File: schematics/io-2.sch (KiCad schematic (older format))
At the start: 9 parts, among them J13 FDC Connector, J9 IDE Connector, U11 WD1772

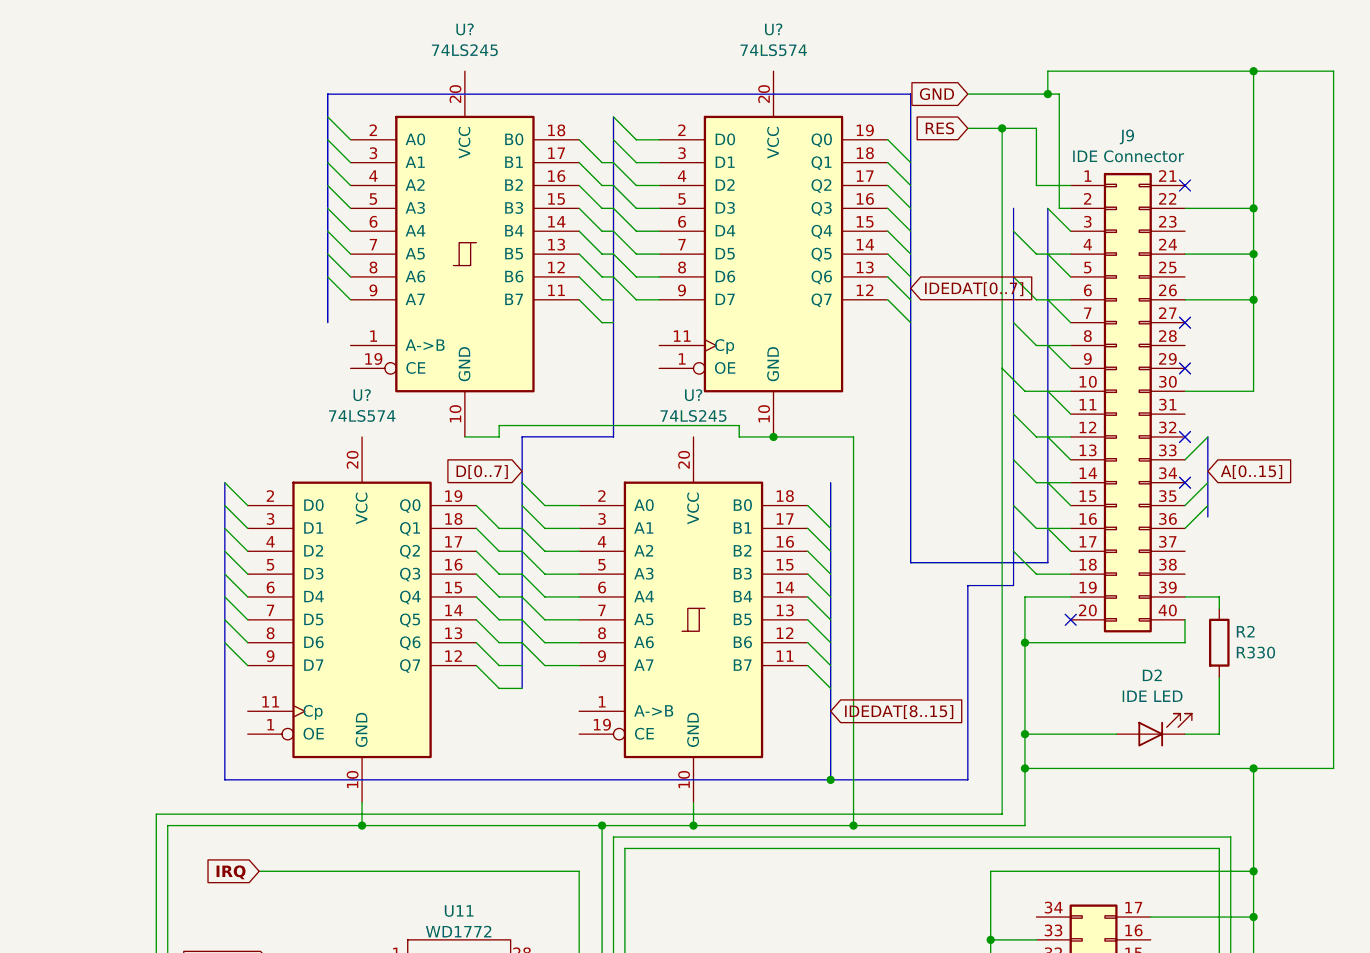
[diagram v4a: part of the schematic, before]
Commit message: Added missing IDE control signals for the latches, bus drivers, reads/writes and chip selects.
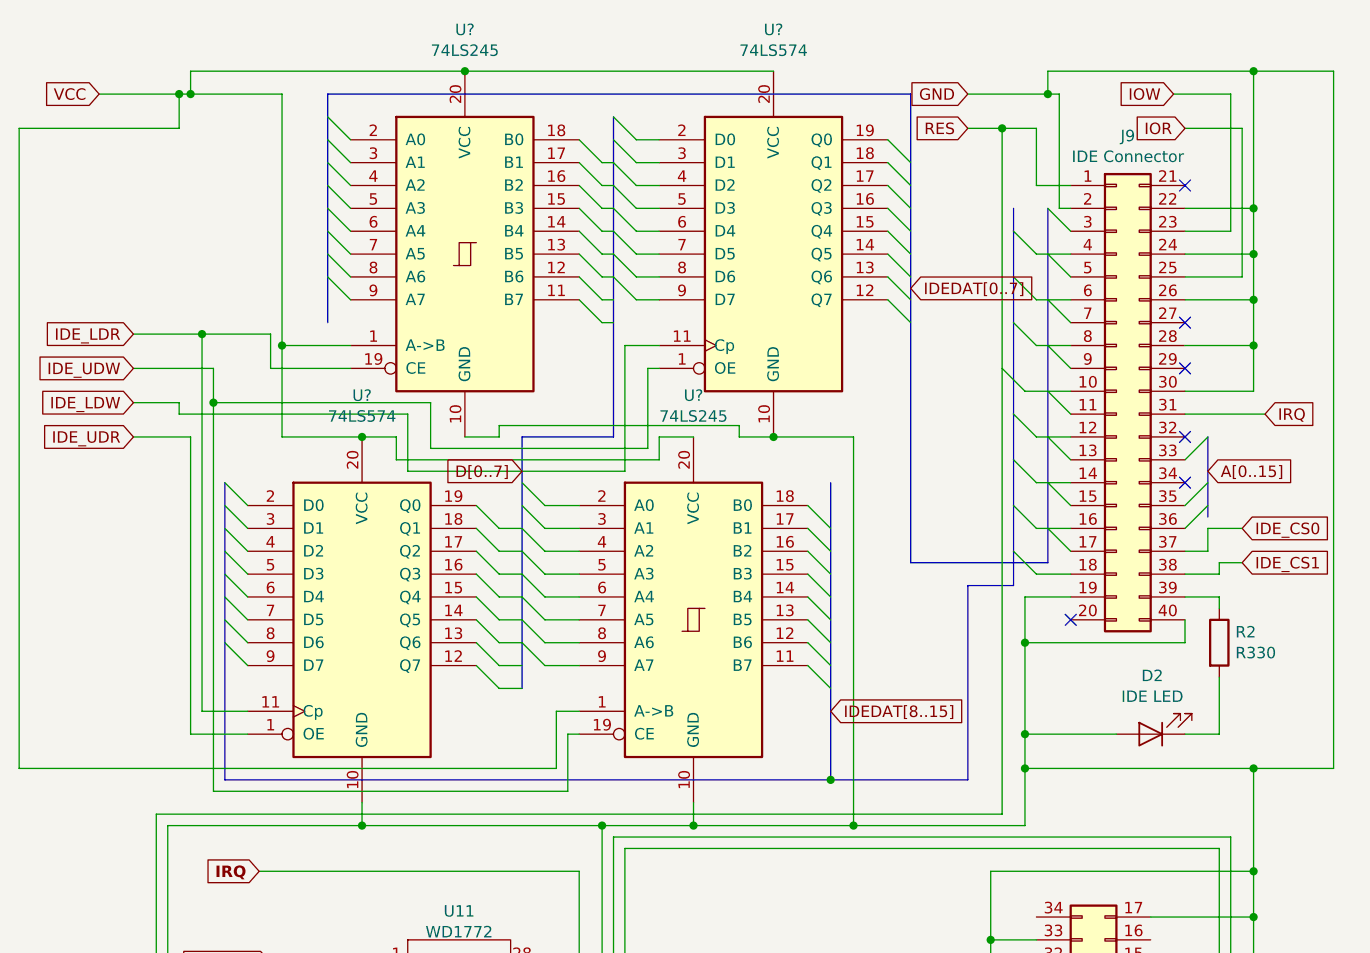
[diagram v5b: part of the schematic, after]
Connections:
- net D[0..7]: now also U?.11 (Cp)
- net GND: now also J9.28 (Pin_28)
- net IRQ: now also J9.31 (Pin_31)
- net VCC: now also U?.1 (A->B), U?.1 (A->B), U?.20 (VCC), U?.20 (VCC), U?.20 (VCC), U?.20 (VCC)
- net IOW: now reaches J9.23 (Pin_23)
- net IOR: now reaches J9.25 (Pin_25)
- net IDE_CS0: now reaches J9.37 (Pin_37)
- net IDE_CS1: now reaches J9.38 (Pin_38)
- net IDE_UDW: now reaches U?.1 (OE)
- net IDE_UDW: now also U?.19 (CE)
- net IDE_UDR: now reaches U?.1 (OE)
- net IDE_LDR: now reaches U?.11 (Cp)
- net IDE_LDR: now also U?.19 (CE)
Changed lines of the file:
@@
 	10500 1950 10800 1950
 Wire Wire Line
-	10800 1950 10800 1550
+	10800 1950 10800 1750
 Connection ~ 10800 1550
 Wire Wire Line
@@
 Wire Wire Line
 	9850 2750 10000 2750
+Text GLabel 5900 1700 0    50   Input ~ 0
+IDE_LDR
+Text GLabel 5750 650  0    50   Input ~ 0
+VCC
+Wire Wire Line
+	8700 550  7350 550
+Wire Wire Line
+	7350 550  6150 550
+Wire Wire Line
+	6150 550  6150 650
+Wire Wire Line
+	6150 650  6100 650
+Connection ~ 7350 550
+Wire Wire Line
+	6550 1750 6550 650
+Wire Wire Line
+	6550 650  6150 650
+Connection ~ 6150 650
+Wire Wire Line
+	6550 1750 6850 1750
+Wire Wire Line
+	7850 3350 7750 3350
+Wire Wire Line
+	7750 3350 7750 3600
+Wire Wire Line
+	7750 3600 5400 3600
+Wire Wire Line
+	5400 3600 5400 800
+Wire Wire Line
+	5400 800  6100 800
+Wire Wire Line
+	6100 800  6100 650
+Connection ~ 6100 650
+Wire Wire Line
+	6100 650  5750 650
+Text GLabel 5900 1850 0    50   Input ~ 0
+IDE_UDW
+Wire Wire Line
+	6850 1850 6500 1850
+Wire Wire Line
+	6500 1850 6500 1700
+Wire Wire Line
+	6500 1700 6200 1700
+Wire Wire Line
+	7850 3450 7800 3450
+Wire Wire Line
+	7800 3450 7800 3700
+Wire Wire Line
+	7800 3700 6250 3700
+Wire Wire Line
+	6250 3700 6250 2000
+Wire Wire Line
+	6250 1850 5900 1850
+Wire Wire Line
+	8200 1850 8150 1850
+Wire Wire Line
+	8150 1850 8150 2200
+Wire Wire Line
+	8150 2200 7200 2200
+Wire Wire Line
+	7200 2200 7200 2000
+Wire Wire Line
+	6900 2150 6550 2150
+Wire Wire Line
+	6550 2150 6550 1750
+Connection ~ 6550 1750
+Wire Wire Line
+	8350 2150 8200 2150
+Wire Wire Line
+	8200 2150 8200 2250
+Wire Wire Line
+	7050 2250 7050 2150
+Wire Wire Line
+	7050 2150 6900 2150
+Connection ~ 6900 2150
+Text GLabel 5900 2150 0    50   Input ~ 0
+IDE_UDR
+Wire Wire Line
+	6400 3450 6150 3450
+Wire Wire Line
+	6150 3450 6150 2150
+Wire Wire Line
+	6150 2150 5900 2150
+Wire Wire Line
+	6400 3350 6200 3350
+Wire Wire Line
+	6200 3350 6200 1700
+Connection ~ 6200 1700
+Wire Wire Line
+	6200 1700 5900 1700
+Wire Wire Line
+	7200 2000 6250 2000
+Connection ~ 6250 2000
+Wire Wire Line
+	6250 2000 6250 1850
+Text GLabel 5900 2000 0    50   Input ~ 0
+IDE_LDW
+Wire Wire Line
+	8200 2250 7050 2250
+Wire Wire Line
+	8200 1750 8050 1750
+Wire Wire Line
+	8050 1750 8050 2300
+Wire Wire Line
+	8050 2300 7100 2300
+Wire Wire Line
+	7100 2300 7100 2050
+Wire Wire Line
+	7100 2050 6100 2050
+Wire Wire Line
+	6100 2050 6100 2000
+Wire Wire Line
+	6100 2000 5900 2000
+Text GLabel 10450 650  0    50   Input ~ 0
+IOW
+Text GLabel 10500 800  0    50   Input ~ 0
+IOR
+Wire Wire Line
+	10450 650  10700 650
+Wire Wire Line
+	10700 650  10700 1250
+Wire Wire Line
+	10700 1250 10500 1250
+Wire Wire Line
+	10500 800  10750 800
+Wire Wire Line
+	10750 800  10750 1450
+Wire Wire Line
+	10750 1450 10500 1450
+Wire Wire Line
+	10500 1750 10800 1750
+Connection ~ 10800 1750
+Wire Wire Line
+	10800 1750 10800 1550
+Text GLabel 10750 2550 2    50   Input ~ 0
+IDE_CS0
+Text GLabel 10750 2700 2    50   Input ~ 0
+IDE_CS1
+Wire Wire Line
+	10750 2550 10600 2550
+Wire Wire Line
+	10600 2550 10600 2650
+Wire Wire Line
+	10600 2650 10500 2650
+Wire Wire Line
+	10750 2700 10650 2700
+Wire Wire Line
+	10650 2700 10650 2750
+Wire Wire Line
+	10650 2750 10500 2750
+Text GLabel 10850 2050 2    50   Input ~ 0
+IRQ
+Wire Wire Line
+	10850 2050 10500 2050
 Wire Wire Line
 	9700 800  9700 3800

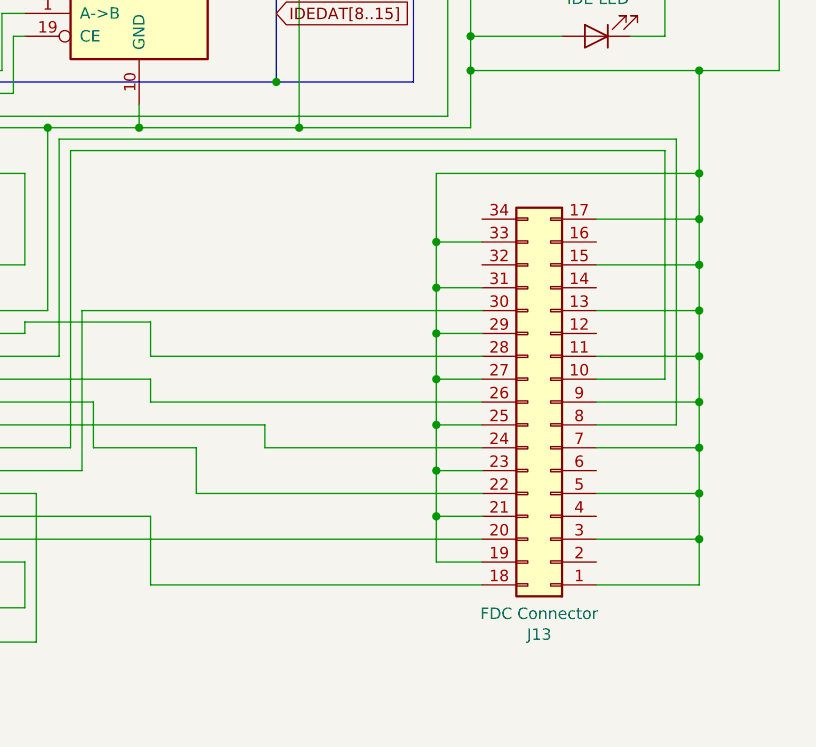
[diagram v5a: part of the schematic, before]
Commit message: Added missing FDC control signals.
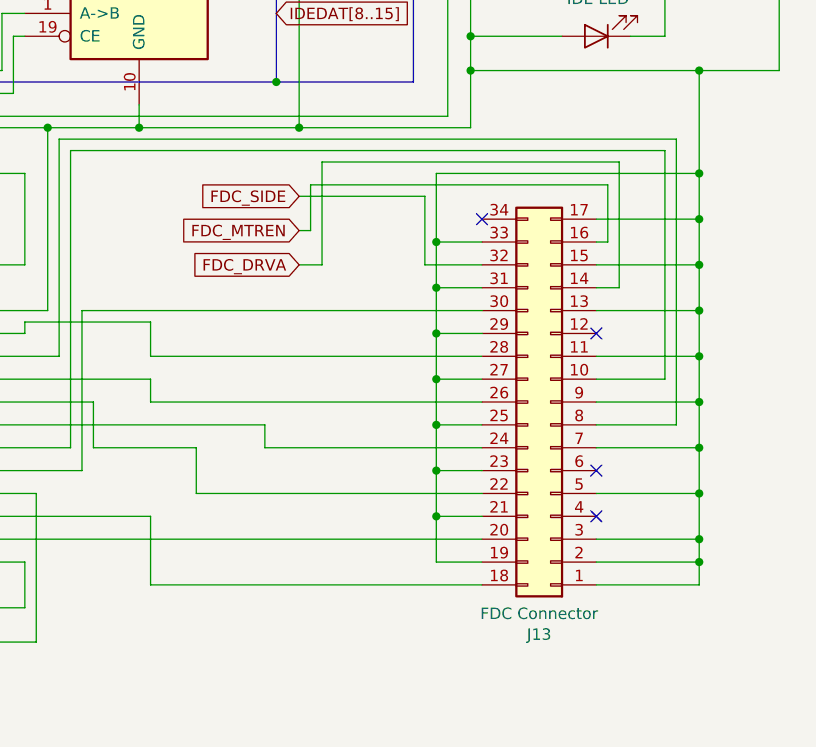
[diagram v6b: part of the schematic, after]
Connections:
- net GND: now also J13.2 (Pin_2)
- net FDC_DRVA: now reaches J13.14 (Pin_14)
- net FDC_MTREN: now reaches J13.16 (Pin_16)
- net FDC_SIDE: now reaches J13.32 (Pin_32)
- no-connect marks 6 -> 10
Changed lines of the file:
@@
 	9700 800  9550 800
 Wire Wire Line
-	10800 5850 10800 5650
+	10800 5850 10800 5750
 Wire Wire Line
 	10350 5850 10800 5850
@@
 Wire Wire Line
 	10850 2050 10500 2050
+NoConn ~ 9850 4250
+Text GLabel 9050 4150 0    50   Input ~ 0
+FDC_SIDE
+Wire Wire Line
+	9850 4450 9600 4450
+Wire Wire Line
+	9600 4450 9600 4150
+Wire Wire Line
+	9600 4150 9050 4150
+Text GLabel 9050 4300 0    50   Input ~ 0
+FDC_MTREN
+Wire Wire Line
+	10350 4350 10400 4350
+Wire Wire Line
+	10400 4350 10400 4100
+Wire Wire Line
+	10400 4100 9100 4100
+Wire Wire Line
+	9100 4100 9100 4300
+Wire Wire Line
+	9100 4300 9050 4300
+Text GLabel 9050 4450 0    50   Input ~ 0
+FDC_DRVA
+Wire Wire Line
+	10450 4550 10450 4000
+Wire Wire Line
+	10450 4000 9150 4000
+Wire Wire Line
+	9150 4000 9150 4450
+Wire Wire Line
+	9150 4450 9050 4450
+Wire Wire Line
+	10350 4550 10450 4550
+NoConn ~ 10350 4750
+NoConn ~ 10350 5350
+NoConn ~ 10350 5550
+Wire Wire Line
+	10350 5750 10800 5750
 Wire Wire Line
 	9700 800  9700 3800
@@
 Wire Bus Line
 	9300 650  9300 2700
+Connection ~ 10800 5750
+Wire Wire Line
+	10800 5750 10800 5650
 $EndSCHEMATC

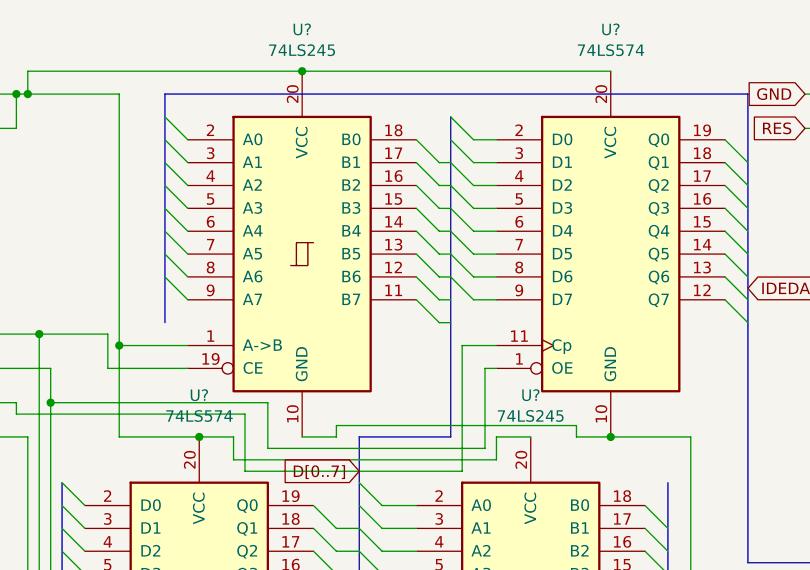
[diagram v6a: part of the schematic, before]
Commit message: Fixes to chip references.
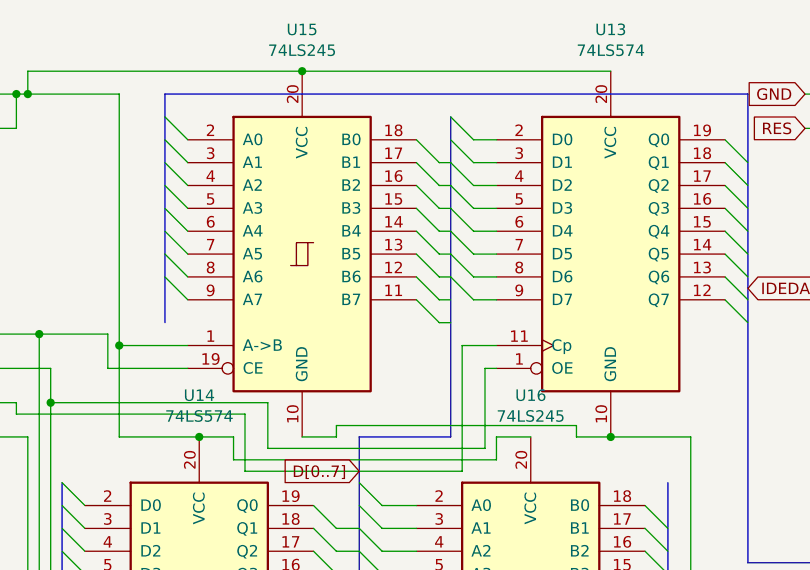
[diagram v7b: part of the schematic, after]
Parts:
- gave numbers to parts that had none: 4
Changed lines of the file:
@@
 	7500 5950 7850 5950
 $Comp
-L 74xx:74LS574 U?
+L 74xx:74LS574 U13
 U 1 1 5EFE16FC
 P 8700 1350
-F 0 "U?" H 8700 2331 50  0000 C CNN
+F 0 "U13" H 8700 2331 50  0000 C CNN
 F 1 "74LS574" H 8700 2240 50  0000 C CNN
 F 2 "" H 8700 1350 50  0001 C CNN
@@
 $EndComp
 $Comp
-L 74xx:74LS574 U?
+L 74xx:74LS574 U14
 U 1 1 5EFE2AF1
 P 6900 2950
-F 0 "U?" H 6900 3931 50  0000 C CNN
+F 0 "U14" H 6900 3931 50  0000 C CNN
 F 1 "74LS574" H 6900 3840 50  0000 C CNN
 F 2 "" H 6900 2950 50  0001 C CNN
@@
 $EndComp
 $Comp
-L 74xx:74LS245 U?
+L 74xx:74LS245 U16
 U 1 1 5EFE3DA1
 P 8350 2950
-F 0 "U?" H 8350 3931 50  0000 C CNN
+F 0 "U16" H 8350 3931 50  0000 C CNN
 F 1 "74LS245" H 8350 3840 50  0000 C CNN
 F 2 "" H 8350 2950 50  0001 C CNN
@@
 $EndComp
 $Comp
-L 74xx:74LS245 U?
+L 74xx:74LS245 U15
 U 1 1 5EFE4D13
 P 7350 1350
-F 0 "U?" H 7350 2331 50  0000 C CNN
+F 0 "U15" H 7350 2331 50  0000 C CNN
 F 1 "74LS245" H 7350 2240 50  0000 C CNN
 F 2 "" H 7350 1350 50  0001 C CNN

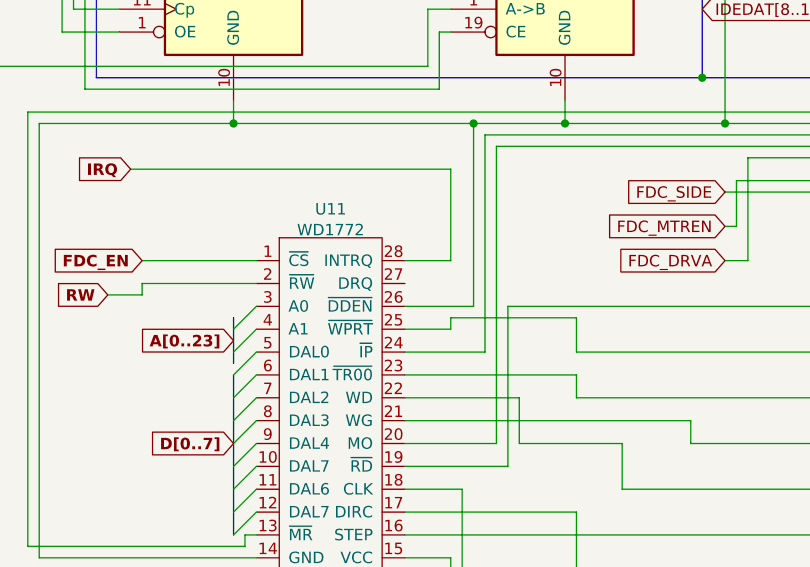
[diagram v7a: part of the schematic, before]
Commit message: Minor tweaks to labels and values.
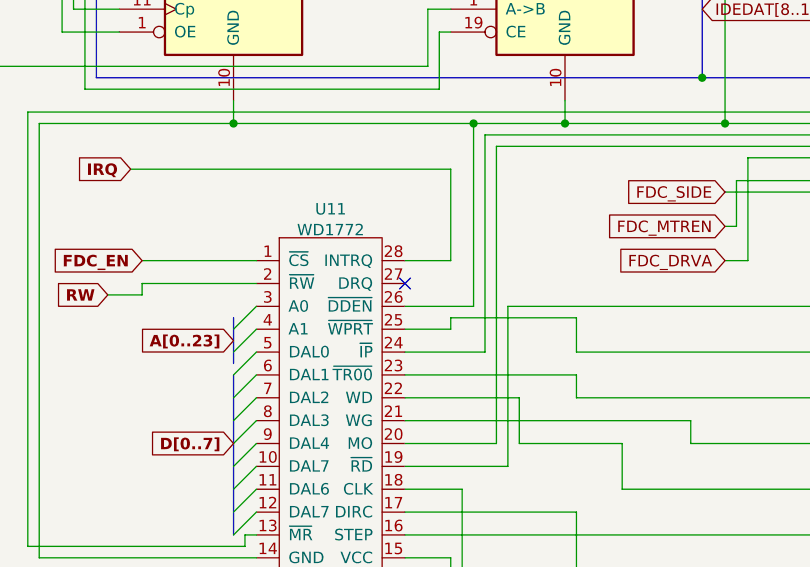
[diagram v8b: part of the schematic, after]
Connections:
- no-connect marks 10 -> 11
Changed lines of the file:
@@
 Wire Wire Line
 	10350 5750 10800 5750
+Connection ~ 10800 5750
+Wire Wire Line
+	10800 5750 10800 5650
+NoConn ~ 7650 4550
 Wire Wire Line
 	9700 800  9700 3800
@@
 Wire Bus Line
 	9300 650  9300 2700
-Connection ~ 10800 5750
-Wire Wire Line
-	10800 5750 10800 5650
 $EndSCHEMATC
